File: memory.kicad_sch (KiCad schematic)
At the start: 7 parts, among them U1 74LS245, U4 74LS04, U5 74LS245, U6 UM6116, U7 27C512, U8 UM6116, U9 74LS138

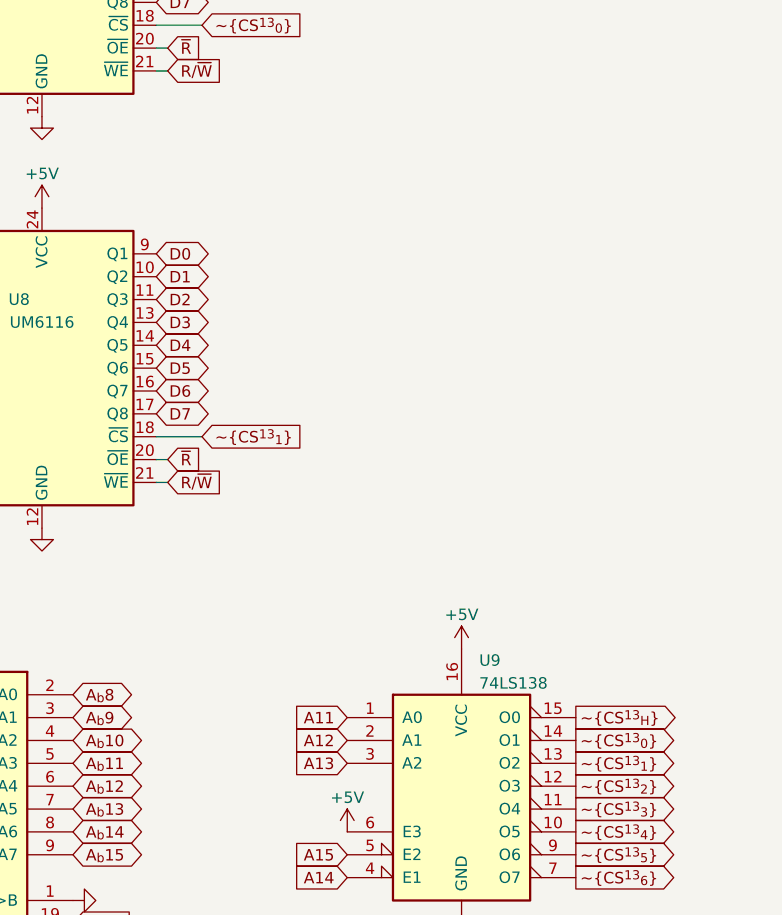
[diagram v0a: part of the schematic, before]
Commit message: add uart
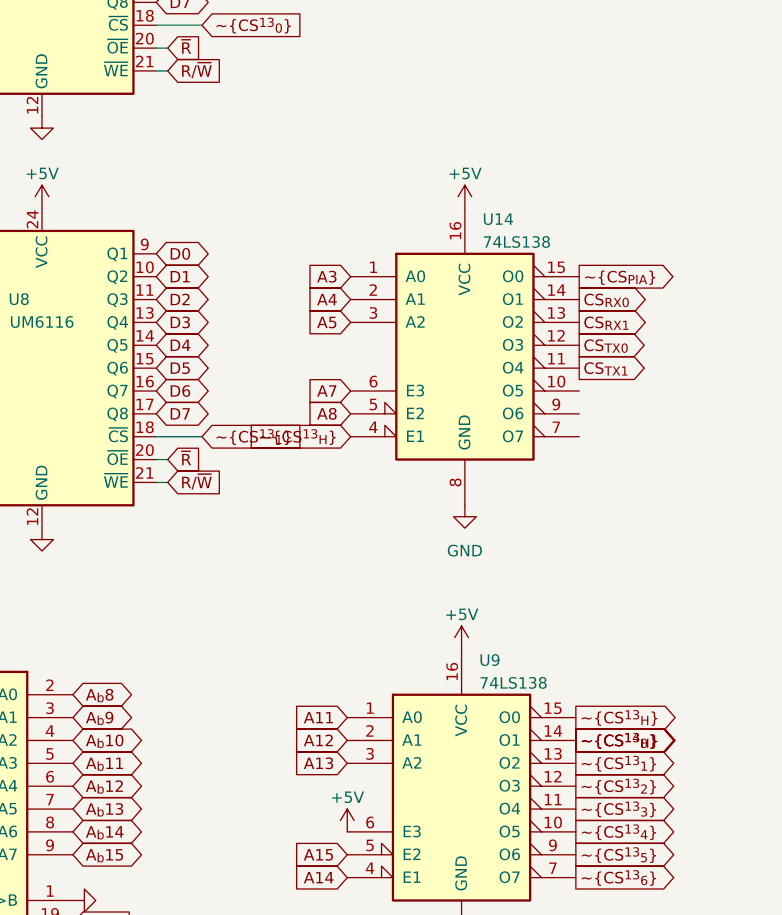
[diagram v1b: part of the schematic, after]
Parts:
- added U14: 74LS138, symbol 74xx:74LS138
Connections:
- net +5V: now also U14.16 (VCC)
- net A3: now also U14.1 (A0)
- net A4: now also U14.2 (A1)
- net A5: now also U14.3 (A2)
- net A7: now also U14.6 (E3)
- net A8: now also U14.5 (E2)
- net GND: now also U14.8 (GND)
- net ~{CS^{13}_{H}}: now also U14.4 (E1)
- new net CS_{RX0}: U14.14 (O1)
- new net CS_{RX1}: U14.13 (O2)
- new net CS_{TX0}: U14.12 (O3)
- new net CS_{TX1}: U14.11 (O4)
- new net ~{CS_{PIA}}: U14.15 (O0)
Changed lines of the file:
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@@
+    )
+  )
+  (global_label "CS_{RX1}" (shape output) (at 167.64 86.36 0) (fields_autoplaced)
+    (effects (font (size 1.27 1.27)) (justify left))
+    (property "Intersheetrefs" "${INTERSHEET_REFS}" (at 175.6839 86.36 0)
+      (effects (font (size 1.27 1.27)) (justify left) hide)
     )
   )
@@
     )
   )
+  (global_label "~{CS^{14}_{H}}" (shape output) (at 167.27 132.81 0) (fields_autoplaced)
+    (effects (font (size 1.27 1.27)) (justify left))
+    (property "Intersheetrefs" "${INTERSHEET_REFS}" (at 175.3562 132.81 0)
+      (effects (font (size 1.27 1.27)) (justify left) hide)
+    )
+  )
   (global_label "D0" (shape tri_state) (at 120.65 33.02 0) (fields_autoplaced)
     (effects (font (size 1.27 1.27)) (justify left))
@@
     )
   )
+  (global_label "A7" (shape input) (at 142.24 93.98 180) (fields_autoplaced)
+    (effects (font (size 1.27 1.27)) (justify right))
+    (property "Intersheetrefs" "${INTERSHEET_REFS}" (at 137.0361 93.98 0)
+      (effects (font (size 1.27 1.27)) (justify right) hide)
+    )
+  )
+  (global_label "A3" (shape input) (at 142.24 81.28 180) (fields_autoplaced)
+    (effects (font (size 1.27 1.27)) (justify right))
+    (property "Intersheetrefs" "${INTERSHEET_REFS}" (at 137.0361 81.28 0)
+      (effects (font (size 1.27 1.27)) (justify right) hide)
+    )
+  )
   (global_label "A8" (shape input) (at 53.34 53.34 180) (fields_autoplaced)
     (effects (font (size 1.27 1.27)) (justify right))
@@
     )
   )
+  (global_label "~{CS^{13}_{H}}" (shape input) (at 142.24 99.06 180) (fields_autoplaced)
+    (effects (font (size 1.27 1.27)) (justify right))
+    (property "Intersheetrefs" "${INTERSHEET_REFS}" (at 134.1538 99.06 0)
+      (effects (font (size 1.27 1.27)) (justify right) hide)
+    )
+  )
   (global_label "A13" (shape input) (at 53.34 66.04 180) (fields_autoplaced)
     (effects (font (size 1.27 1.27)) (justify right))
@@
     )
   )
+  (global_label "CS_{TX1}" (shape output) (at 167.64 91.44 0) (fields_autoplaced)
+    (effects (font (size 1.27 1.27)) (justify left))
+    (property "Intersheetrefs" "${INTERSHEET_REFS}" (at 175.4722 91.44 0)
+      (effects (font (size 1.27 1.27)) (justify left) hide)
+    )
+  )
   (global_label "D6" (shape tri_state) (at 120.65 93.98 0) (fields_autoplaced)
     (effects (font (size 1.27 1.27)) (justify left))
@@
     )
   )
+  (global_label "CS_{RX0}" (shape output) (at 167.64 83.82 0) (fields_autoplaced)
+    (effects (font (size 1.27 1.27)) (justify left))
+    (property "Intersheetrefs" "${INTERSHEET_REFS}" (at 175.6839 83.82 0)
+      (effects (font (size 1.27 1.27)) (justify left) hide)
+    )
+  )
+  (global_label "A8" (shape input) (at 142.24 96.52 180) (fields_autoplaced)
+    (effects (font (size 1.27 1.27)) (justify right))
+    (property "Intersheetrefs" "${INTERSHEET_REFS}" (at 137.0361 96.52 0)
+      (effects (font (size 1.27 1.27)) (justify right) hide)
+    )
+  )
   (global_label "A11" (shape input) (at 85.99 135.35 180) (fields_autoplaced)
     (effects (font (size 1.27 1.27)) (justify right))
@@
     )
   )
+  (global_label "CS_{TX0}" (shape output) (at 167.64 88.9 0) (fields_autoplaced)
+    (effects (font (size 1.27 1.27)) (justify left))
+    (property "Intersheetrefs" "${INTERSHEET_REFS}" (at 175.4722 88.9 0)
+      (effects (font (size 1.27 1.27)) (justify left) hide)
+    )
+  )
   (global_label "A9" (shape input) (at 53.34 55.88 180) (fields_autoplaced)
     (effects (font (size 1.27 1.27)) (justify right))
@@
     )
   )
+  (global_label "~{CS_{PIA}}" (shape output) (at 167.64 81.28 0) (fields_autoplaced)
+    (effects (font (size 1.27 1.27)) (justify left))
+    (property "Intersheetrefs" "${INTERSHEET_REFS}" (at 175.1758 81.28 0)
+      (effects (font (size 1.27 1.27)) (justify left) hide)
+    )
+  )
   (global_label "A0" (shape input) (at 53.34 33.02 180) (fields_autoplaced)
     (effects (font (size 1.27 1.27)) (justify right))
@@
     )
   )
+  (global_label "A4" (shape input) (at 142.24 83.82 180) (fields_autoplaced)
+    (effects (font (size 1.27 1.27)) (justify right))
+    (property "Intersheetrefs" "${INTERSHEET_REFS}" (at 137.0361 83.82 0)
+      (effects (font (size 1.27 1.27)) (justify right) hide)
+    )
+  )
   (global_label "A_{b}10" (shape tri_state) (at 95.25 104.14 180) (fields_autoplaced)
     (effects (font (size 1.27 1.27)) (justify right))
@@
     (property "Intersheetrefs" "${INTERSHEET_REFS}" (at 67.6758 107.95 0)
       (effects (font (size 1.27 1.27)) (justify left) hide)
+    )
+  )
+  (global_label "A5" (shape input) (at 142.24 86.36 180) (fields_autoplaced)
+    (effects (font (size 1.27 1.27)) (justify right))
+    (property "Intersheetrefs" "${INTERSHEET_REFS}" (at 137.0361 86.36 0)
+      (effects (font (size 1.27 1.27)) (justify right) hide)
     )
   )
@@
         (path "/e63e39d7-6ac0-4ffd-8aa3-1841a4541b55/bfe21baf-1342-48ad-994b-20326b13bad2"
           (reference "#PWR018") (unit 1)
+        )
+      )
+    )
+  )
+  (symbol (lib_name "GND_1") (lib_id "power:GND") (at 154.94 106.68 0) (unit 1)
+    (in_bom yes) (on_board yes) (dnp no) (fields_autoplaced)
+    (property "Reference" "#PWR036" (at 154.94 113.03 0)
+      (effects (font (size 1.27 1.27)) hide)
+    )
+    (property "Value" "GND" (at 154.94 111.76 0)
+      (effects (font (size 1.27 1.27)))
+    )
+    (property "Footprint" "" (at 154.94 106.68 0)
+      (effects (font (size 1.27 1.27)) hide)
+    )
+    (property "Datasheet" "" (at 154.94 106.68 0)
+      (effects (font (size 1.27 1.27)) hide)
+    )
+    (pin "1")
+    (instances
+      (project "6802 v1"
+        (path "/e63e39d7-6ac0-4ffd-8aa3-1841a4541b55/aacad567-86ad-4193-8aa8-08565ab103a5"
+          (reference "#PWR036") (unit 1)
+        )
+        (path "/e63e39d7-6ac0-4ffd-8aa3-1841a4541b55/bfe21baf-1342-48ad-994b-20326b13bad2"
+          (reference "#PWR031") (unit 1)
         )
       )
@@
         )
       )
+    )
+  )
+  (symbol (lib_name "+5V_1") (lib_id "power:+5V") (at 154.94 73.66 0) (unit 1)
+    (in_bom yes) (on_board yes) (dnp no) (fields_autoplaced)
+    (property "Reference" "#PWR030" (at 154.94 77.47 0)
+      (effects (font (size 1.27 1.27)) hide)
+    )
+    (property "Value" "+5V" (at 154.94 69.85 0)
+      (effects (font (size 1.27 1.27)))
+    )
+    (property "Footprint" "" (at 154.94 73.66 0)
+      (effects (font (size 1.27 1.27)) hide)
+    )
+    (property "Datasheet" "" (at 154.94 73.66 0)
+      (effects (font (size 1.27 1.27)) hide)
+    )
+    (pin "1")
+    (instances
+      (project "6802 v1"
+        (path "/e63e39d7-6ac0-4ffd-8aa3-1841a4541b55/aacad567-86ad-4193-8aa8-08565ab103a5"
+          (reference "#PWR030") (unit 1)
+        )
+        (path "/e63e39d7-6ac0-4ffd-8aa3-1841a4541b55/bfe21baf-1342-48ad-994b-20326b13bad2"
+          (reference "#PWR030") (unit 1)
+        )
+      )
+    )
+  )
+  (symbol (lib_id "74xx:74LS138") (at 154.94 88.9 0) (unit 1)
+    (in_bom yes) (on_board yes) (dnp no) (fields_autoplaced)
+    (property "Reference" "U14" (at 156.8959 74.93 0)
+      (effects (font (size 1.27 1.27)) (justify left))
+    )
+    (property "Value" "74LS138" (at 156.8959 77.47 0)
+      (effects (font (size 1.27 1.27)) (justify left))
+    )
+    (property "Footprint" "" (at 154.94 88.9 0)
+      (effects (font (size 1.27 1.27)) hide)
+    )
+    (property "Datasheet" "http://www.ti.com/lit/gpn/sn74LS138" (at 154.94 88.9 0)
+      (effects (font (size 1.27 1.27)) hide)
+    )
+    (pin "1")
+    (pin "10")
+    (pin "11")
+    (pin "12")
+    (pin "13")
+    (pin "14")
+    (pin "15")
+    (pin "16")
+    (pin "2")
+    (pin "3")
+    (pin "4")
+    (pin "5")
+    (pin "6")
+    (pin "7")
+    (pin "8")
+    (pin "9")
+    (instances
+      (project "6802 v1"
+        (path "/e63e39d7-6ac0-4ffd-8aa3-1841a4541b55/aacad567-86ad-4193-8aa8-08565ab103a5"
+          (reference "U14") (unit 1)
+        )
+        (path "/e63e39d7-6ac0-4ffd-8aa3-1841a4541b55/bfe21baf-1342-48ad-994b-20326b13bad2"
+          (reference "U12") (unit 1)
+        )
+      )
